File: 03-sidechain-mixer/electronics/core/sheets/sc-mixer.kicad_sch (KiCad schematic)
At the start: 56 parts, among them Q1 BC847BS, U1 TL072, U2 TL072, U3 TL072, U4 TL072

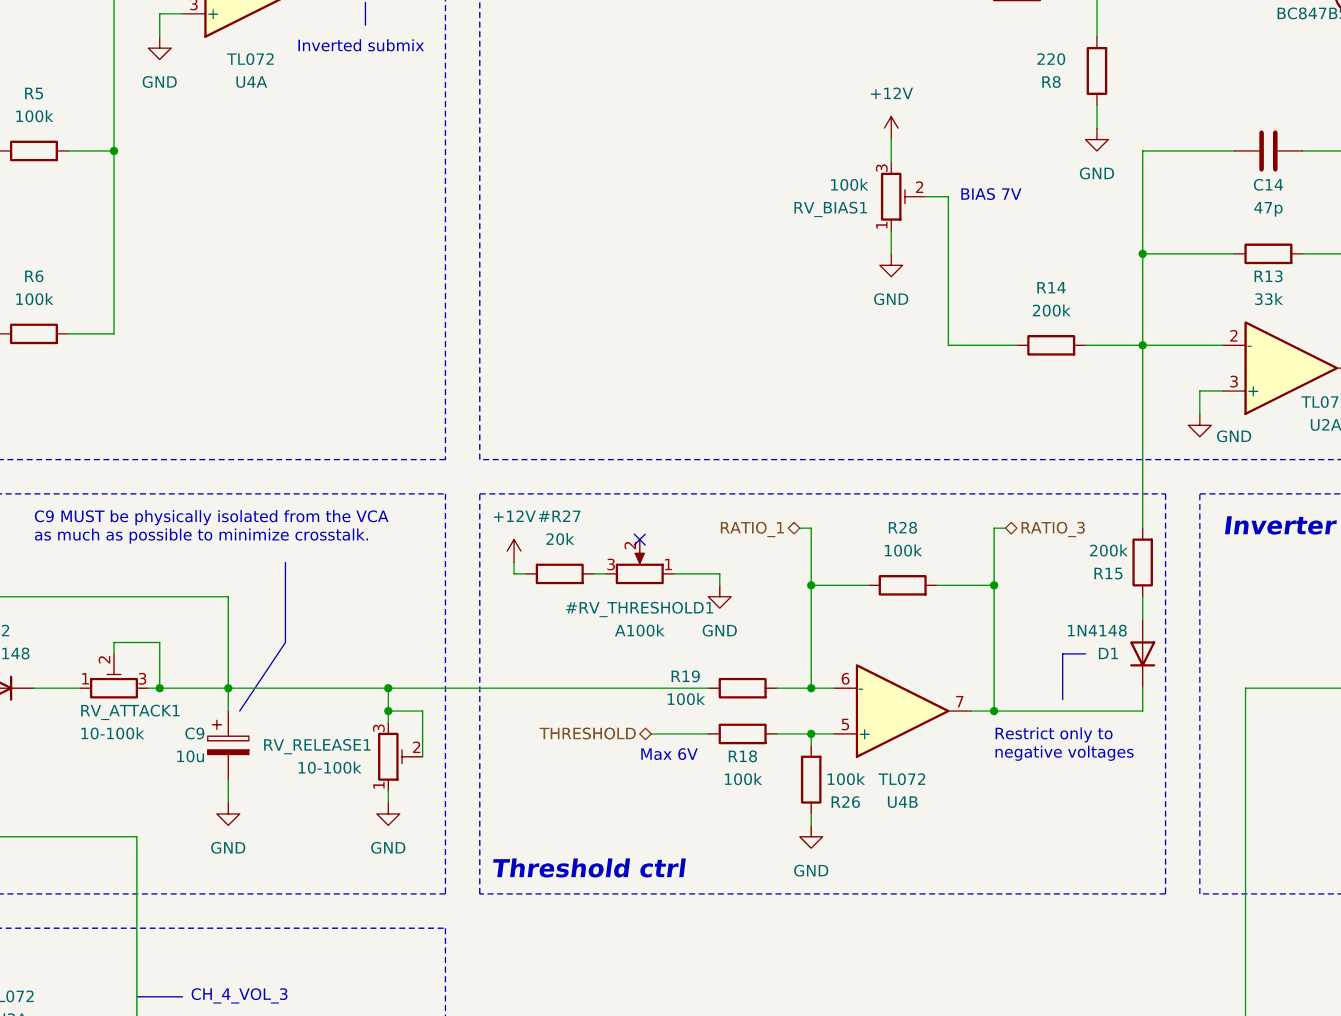
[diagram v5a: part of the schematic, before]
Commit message: Added SC Mixer UI schematics
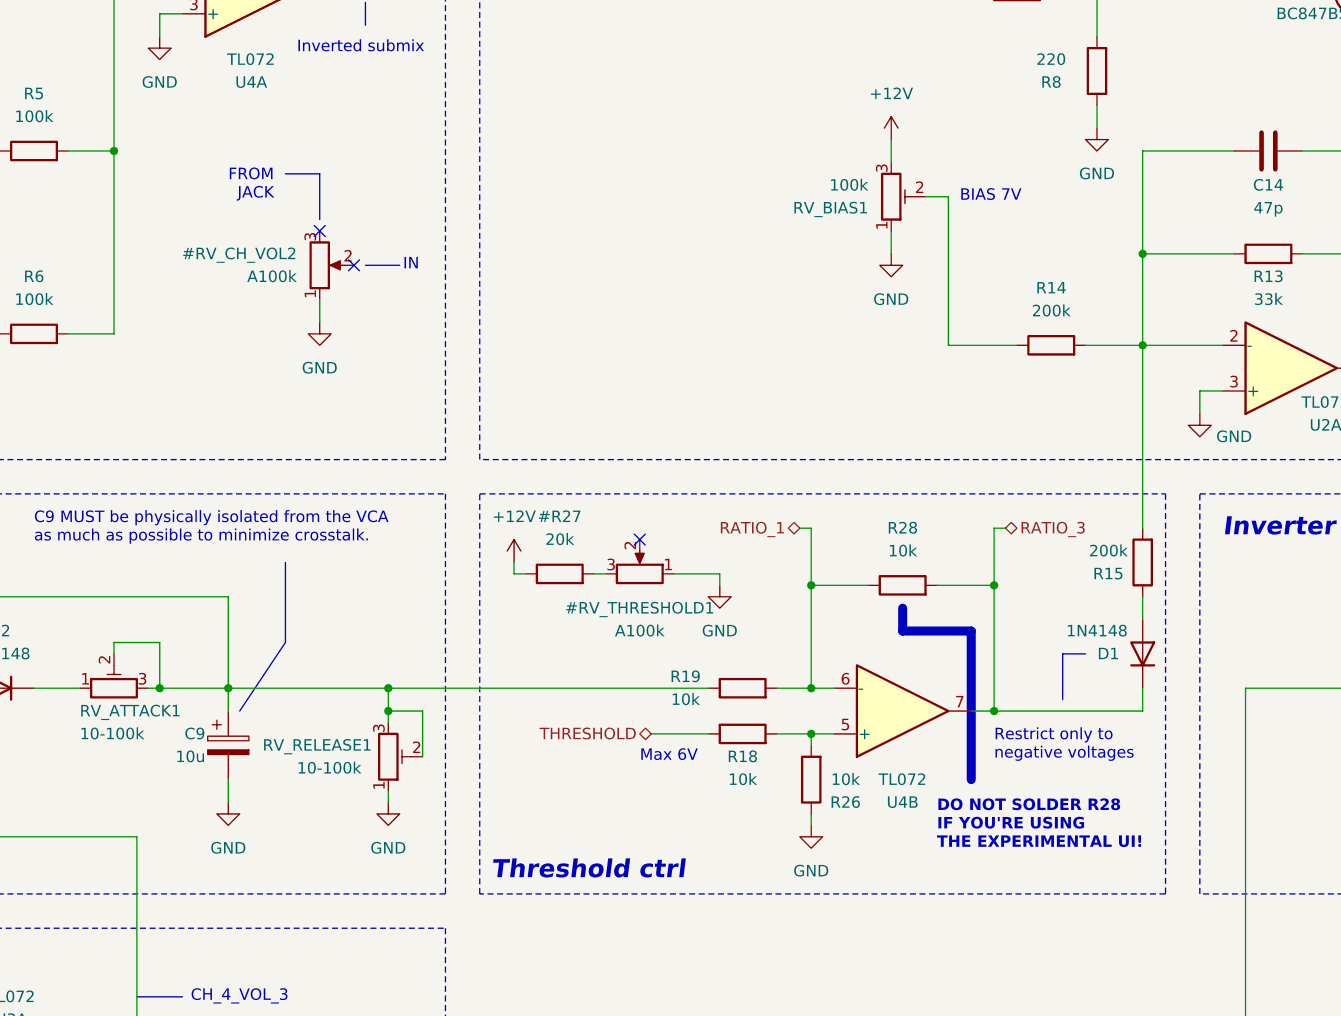
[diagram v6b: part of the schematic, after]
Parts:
- added #RV_CH_VOL2: A100k, symbol Device:R_Potentiometer
- R18, R19, R26, R28: value 100k -> 10k
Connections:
- net GND: now also #RV_CH_VOL2.1
- no-connect marks 5 -> 7
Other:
- note added: "DO NOT SOLDER R28 IF YOU'RE USING THE EXPERIMENTAL UI!"
- note added: "FROM JACK"
- note added: "IN"

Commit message: Checked all components on SC-Mixer
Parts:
- C1, C10, C11, C12, C13, C14, C2, C3, C4, C5, C6, C7, C8, C9, Q1, R1, R10, R11, R12, R13, R14, R15, R16, R17, R2, R21, R22, R23, R24, R3, R4, R5, R6, R7, R8, R9, U1, U2, U3, U4: CHECKED (none) -> YES
- D1, D2: footprint Diode_SMD:D_SOD-323_HandSoldering -> Diode_SMD:D_SOD-123; CHECKED (none) -> YES; LCSC C2128 -> C81598; Vendor (none) -> JLCPCB
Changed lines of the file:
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@@
 			)
 		)
-		(property "CHECKED" ""
+		(property "CHECKED" "YES"
 			(at 314.96 44.45 90)
 			(effects
@@
 			)
 		)
-		(property "CHECKED" ""
+		(property "CHECKED" "YES"
 			(at 218.44 52.07 0)
 			(effects
@@
 			)
 		)
-		(property "CHECKED" ""
+		(property "CHECKED" "YES"
 			(at 190.5 193.04 0)
 			(effects
@@
 			)
 		)
-		(property "CHECKED" ""
+		(property "CHECKED" "YES"
 			(at 297.18 44.45 0)
 			(effects
@@
 			)
 		)
-		(property "CHECKED" ""
+		(property "CHECKED" "YES"
 			(at 118.11 196.85 0)
 			(effects
@@
 			)
 		)
-		(property "CHECKED" ""
+		(property "CHECKED" "YES"
 			(at 146.05 132.08 0)
 			(effects
@@
 			)
 		)
-		(property "CHECKED" ""
+		(property "CHECKED" "YES"
 			(at 73.66 52.07 0)
 			(effects
@@
 			)
 		)
+		(property "CHECKED" "YES"
+			(at 45.72 171.45 0)
+			(effects
+				(font
+					(size 1.27 1.27)
+				)
+				(hide yes)
+			)
+		)
 		(pin "2"
 		)
@@
 			)
 		)
-		(property "CHECKED" ""
+		(property "CHECKED" "YES"
 			(at 167.64 200.66 0)
 			(effects
@@
 			)
 		)
-		(property "CHECKED" ""
+		(property "CHECKED" "YES"
 			(at 207.01 73.66 90)
 			(effects
@@
 			)
 		)
-		(property "CHECKED" ""
+		(property "CHECKED" "YES"
 			(at 156.21 200.66 0)
 			(effects
@@
 			)
 		)
-		(property "CHECKED" ""
+		(property "CHECKED" "YES"
 			(at 228.6 121.92 90)
 			(effects
@@
 			)
 		)
+		(property "CHECKED" "YES"
+			(at 248.92 19.05 90)
+			(effects
+				(font
+					(size 1.27 1.27)
+				)
+				(hide yes)
+			)
+		)
 		(pin "1"
 		)
@@
 			)
 		)
-		(property "CHECKED" ""
+		(property "CHECKED" "YES"
 			(at 179.07 200.66 0)
 			(effects
@@
 			)
 		)
+		(property "CHECKED" "YES"
+			(at 71.12 135.89 0)
+			(effects
+				(font
+					(size 1.27 1.27)
+				)
+				(hide yes)
+			)
+		)
 		(pin "1"
 		)
@@
 			)
 		)
+		(property "CHECKED" "YES"
+			(at 33.02 129.54 0)
+			(effects
+				(font
+					(size 1.27 1.27)
+				)
+				(hide yes)
+			)
+		)
 		(pin "2"
 		)
@@
 			)
 		)
-		(property "CHECKED" ""
+		(property "CHECKED" "YES"
 			(at 49.53 69.85 90)
 			(effects
@@
 			)
 		)
-		(property "CHECKED" ""
+		(property "CHECKED" "YES"
 			(at 248.92 41.91 0)
 			(effects
@@
 			)
 		)
-		(property "CHECKED" ""
+		(property "CHECKED" "YES"
 			(at 232.41 39.37 90)
 			(effects
@@
 			)
 		)
-		(property "Footprint" "Diode_SMD:D_SOD-323_HandSoldering"
+		(property "Footprint" "Diode_SMD:D_SOD-123"
 			(at 45.72 129.54 0)
 			(effects
@@
 			)
 		)
-		(property "LCSC" "C2128"
+		(property "LCSC" "C81598"
 			(at 45.72 129.54 0)
 			(effects
@@
 			)
 		)
-		(property "Vendor" ""
+		(property "Vendor" "JLCPCB"
+			(at 45.72 129.54 0)
+			(effects
+				(font
+					(size 1.27 1.27)
+				)
+				(hide yes)
+			)
+		)
+		(property "CHECKED" "YES"
 			(at 45.72 129.54 0)
 			(effects
@@
 			)
 		)
-		(property "CHECKED" ""
+		(property "CHECKED" "YES"
 			(at 198.12 34.29 90)
 			(effects
@@
 			)
 		)
-		(property "CHECKED" ""
+		(property "CHECKED" "YES"
 			(at 190.5 200.66 0)
 			(effects
@@
 			)
 		)
-		(property "CHECKED" ""
+		(property "CHECKED" "YES"
 			(at 189.23 93.98 0)
 			(effects
@@
 			)
 		)
-		(property "CHECKED" ""
+		(property "CHECKED" "YES"
 			(at 74.93 40.64 90)
 			(effects
@@
 			)
 		)
+		(property "CHECKED" "YES"
+			(at 128.27 196.85 0)
+			(effects
+				(font
+					(size 1.27 1.27)
+				)
+				(hide yes)
+			)
+		)
 		(pin "2"
 		)
@@
 			)
 		)
-		(property "CHECKED" ""
+		(property "CHECKED" "YES"
 			(at 248.92 29.21 90)
 			(effects
@@
 			)
 		)
-		(property "CHECKED" ""
+		(property "CHECKED" "YES"
 			(at 167.64 193.04 0)
 			(effects
@@
 			)
 		)
-		(property "CHECKED" ""
+		(property "CHECKED" "YES"
 			(at 238.76 54.61 90)
 			(effects
@@
 			)
 		)
-		(property "CHECKED" ""
+		(property "CHECKED" "YES"
 			(at 49.53 49.53 90)
 			(effects
@@
 			)
 		)
+		(property "CHECKED" "YES"
+			(at 228.6 111.76 90)
+			(effects
+				(font
+					(size 1.27 1.27)
+				)
+				(hide yes)
+			)
+		)
 		(pin "1"
 		)
@@
 			)
 		)
-		(property "CHECKED" ""
+		(property "CHECKED" "YES"
 			(at 195.58 52.07 0)
 			(effects
@@
 			)
 		)
-		(property "CHECKED" ""
+		(property "CHECKED" "YES"
 			(at 215.9 34.29 90)
 			(effects
@@
 			)
 		)
-		(property "Footprint" "Diode_SMD:D_SOD-323_HandSoldering"
+		(property "Footprint" "Diode_SMD:D_SOD-123"
 			(at 172.72 125.73 0)
 			(effects
@@
 			)
 		)
-		(property "LCSC" "C2128"
+		(property "LCSC" "C81598"
 			(at 172.72 125.73 90)
 			(effects
@@
 			)
 		)
-		(property "Vendor" ""
+		(property "Vendor" "JLCPCB"
 			(at 172.72 125.73 0)
 			(effects
@@
 			)
 		)
+		(property "CHECKED" "YES"
+			(at 172.72 125.73 90)
+			(effects
+				(font
+					(size 1.27 1.27)
+				)
+				(hide yes)
+			)
+		)
 		(pin "1"
 		)
@@
 			)
 		)
-		(property "CHECKED" ""
+		(property "CHECKED" "YES"
 			(at 138.43 196.85 0)
 			(effects
@@
 			)
 		)
-		(property "CHECKED" ""
+		(property "CHECKED" "YES"
 			(at 207.01 129.54 90)
 			(effects
@@
 			)
 		)
-		(property "CHECKED" ""
+		(property "CHECKED" "YES"
 			(at 283.21 63.5 90)
 			(effects
@@
 			)
 		)
+		(property "CHECKED" "YES"
+			(at 74.93 27.94 90)
+			(effects
+				(font
+					(size 1.27 1.27)
+				)
+				(hide yes)
+			)
+		)
 		(pin "1"
 		)
@@
 			)
 		)
-		(property "CHECKED" ""
+		(property "CHECKED" "YES"
 			(at 148.59 196.85 0)
 			(effects
@@
 			)
 		)
-		(property "CHECKED" ""
+		(property "CHECKED" "YES"
 			(at 167.64 60.96 90)
 			(effects
@@
 			)
 		)
-		(property "CHECKED" ""
+		(property "CHECKED" "YES"
 			(at 179.07 193.04 0)
 			(effects
@@
 			)
 		)
-		(property "CHECKED" ""
+		(property "CHECKED" "YES"
 			(at 228.6 132.08 0)
 			(effects
@@
 			)
 		)
-		(property "CHECKED" ""
+		(property "CHECKED" "YES"
 			(at 158.75 52.07 90)
 			(effects
@@
 			)
 		)
-		(property "CHECKED" ""
+		(property "CHECKED" "YES"
 			(at 232.41 44.45 90)
 			(effects
@@
 			)
 		)
-		(property "CHECKED" ""
+		(property "CHECKED" "YES"
 			(at 172.72 115.57 90)
 			(effects
@@
 			)
 		)
+		(property "CHECKED" "YES"
+			(at 295.91 19.05 90)
+			(effects
+				(font
+					(size 1.27 1.27)
+				)
+				(hide yes)
+			)
+		)
 		(pin "1"
 		)
@@
 			)
 		)
+		(property "CHECKED" "YES"
+			(at 186.69 69.85 90)
+			(effects
+				(font
+					(size 1.27 1.27)
+				)
+				(hide yes)
+			)
+		)
 		(pin "1"
 		)
@@
 			)
 		)
-		(property "CHECKED" ""
+		(property "CHECKED" "YES"
 			(at 49.53 90.17 90)
 			(effects
@@
 			)
 		)
-		(property "CHECKED" ""
+		(property "CHECKED" "YES"
 			(at 162.56 91.44 90)
 			(effects
@@
 			)
 		)
-		(property "CHECKED" ""
+		(property "CHECKED" "YES"
 			(at 156.21 193.04 0)
 			(effects
@@
 			)
 		)
-		(property "CHECKED" ""
+		(property "CHECKED" "YES"
 			(at 186.69 81.28 90)
 			(effects
@@
 			)
 		)
-		(property "CHECKED" ""
+		(property "CHECKED" "YES"
 			(at 273.05 41.91 90)
 			(effects

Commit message: ADSR-VCA first stab
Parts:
- C9: footprint Capacitor_SMD:CP_Elec_4x5.4 -> Capacitor_SMD:CP_Elec_5x5.4; LCSC C72485 -> C30110
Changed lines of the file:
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@@
 			)
 		)
-		(property "Footprint" "Capacitor_SMD:CP_Elec_4x5.4"
+		(property "Footprint" "Capacitor_SMD:CP_Elec_5x5.4"
 			(at 72.0852 139.7 0)
 			(effects
@@
 			)
 		)
-		(property "LCSC" "C72485"
+		(property "LCSC" "C30110"
 			(at 71.12 135.89 0)
 			(effects
@@
 			)
 		)
+		(property "Part No." ""
+			(at 71.12 135.89 0)
+			(effects
+				(font
+					(size 1.27 1.27)
+				)
+				(hide yes)
+			)
+		)
+		(property "Part URL" ""
+			(at 71.12 135.89 0)
+			(effects
+				(font
+					(size 1.27 1.27)
+				)
+				(hide yes)
+			)
+		)
 		(pin "1"
 		)
@@
 			)
 		)
+		(property "Part No." ""
+			(at 88.9 137.16 0)
+			(effects
+				(font
+					(size 1.27 1.27)
+				)
+				(hide yes)
+			)
+		)
+		(property "Part URL" ""
+			(at 88.9 137.16 0)
+			(effects
+				(font
+					(size 1.27 1.27)
+				)
+				(hide yes)
+			)
+		)
+		(property "Vendor" ""
+			(at 88.9 137.16 0)
+			(effects
+				(font
+					(size 1.27 1.27)
+				)
+				(hide yes)
+			)
+		)
 		(pin "2"
 		)
@@
 			(effects
 				(font
+					(size 1.27 1.27)
+				)
+				(hide yes)
+			)
+		)
+		(property "Part No." ""
+			(at 58.42 129.54 0)
+			(effects
+				(font
+					(size 1.27 1.27)
+				)
+				(hide yes)
+			)
+		)
+		(property "Part URL" ""
+			(at 58.42 129.54 0)
+			(effects
+				(font
+					(size 1.27 1.27)
+				)
+				(hide yes)
+			)
+		)
+		(property "Vendor" ""
+			(at 58.42 129.54 0)
+			(effects
+				(font
